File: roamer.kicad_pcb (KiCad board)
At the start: 4 copper layers, 39 x 99 mm, 103 parts, among them J1 Conn_Coaxial_Small, J2 JSTPH, J3 Conn_02x05_Odd_Even, J4 Conn_Coaxial_Small, J5 Conn_02x05_Odd_Even, J8 MEM2075-00-140-01-A, Q3 DMP2070UQ-7, SW1 KMR2, U1 2MB Flash, U2 AP2112K-3.3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

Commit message: Adding finishing touches
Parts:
- removed TP7, TP8, TP9: TestPoint, TestPoint:TestPoint_Loop_D2.50mm_Drill1.0mm
- added +BAT: TestPoint, TestPoint:TestPoint_Loop_D2.50mm_Drill1.0mm, F.Cu at (253.0, 174.8)
- added +VBUS: TestPoint, TestPoint:TestPoint_Loop_D2.50mm_Drill1.0mm, F.Cu at (253.0, 170.2)
- added 3V3: TestPoint, TestPoint:TestPoint_Loop_D2.50mm_Drill1.0mm, F.Cu at (240.0, 173.5)
- added G***: LOGO, LOGO, F.Cu at (236.2, 169.2)
- AREF <> 3V3: renamed from JP1
- IN <> +BATT: renamed from JP3
- LoRa 433: renamed from U9
- LoRa 900: renamed from U4
- moved R9 3.64 mm to (221.0, 164.2)
- renumbered U7 to BME, U8 to INA
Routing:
- net /Power - Management/IN-: track 27.2 -> 17.3 mm
- net VBUS: track 58.3 -> 65.8 mm
- net Net-(MCU1-PB01): track 20.2 -> 16.5 mm
- net +BATT: track 85.2 -> 82.6 mm, vias 2 -> 3
- net GND: track 147.2 -> 147.4 mm, vias 118 -> 115
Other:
- board text added: "433 Mhz"
- board text added: "900 Mhz"
- board text added: "BATT"
- board text added: "ROAMER"
- board text added: "SWD"
- board text added: "catbranchman"
- board text added: "rev 1"

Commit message: Creating fab package
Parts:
- added TP6: GND Testpoint, TestPoint:TestPoint_Loop_D2.50mm_Drill1.0mm, F.Cu at (221.8, 156.2)
- JP1: renamed from AREF <> 3V3
- JP3: renamed from IN <> +BATT
- TP1: renamed from +VBUS; value TestPoint -> VBUS Testpoint
- TP2: renamed from +BAT; value TestPoint -> Batt Testpoint
- TP3: value TestPoint -> D+ Testpoint
- TP4: value TestPoint -> D- TestPoint
- TP7: renamed from 3V3; value TestPoint -> 3V3 Testpoint
- U4: renamed from LoRa 900
- U9: renamed from LoRa 433
- moved G*** 0.25 mm to (236.0, 169.2)
- renumbered BME to U7, INA to U8
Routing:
- net GND: track 147.4 -> 151.1 mm, vias 115 -> 108
- net Net-(MCU1-PB01): track 16.5 -> 20.2 mm
- net /Bus - SPI/SPI.SCK: track 62.3 -> 63.9 mm
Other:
- board text added: "433M"
- board text added: "915M"
- board text removed: "433 Mhz"
- board text removed: "900 Mhz"

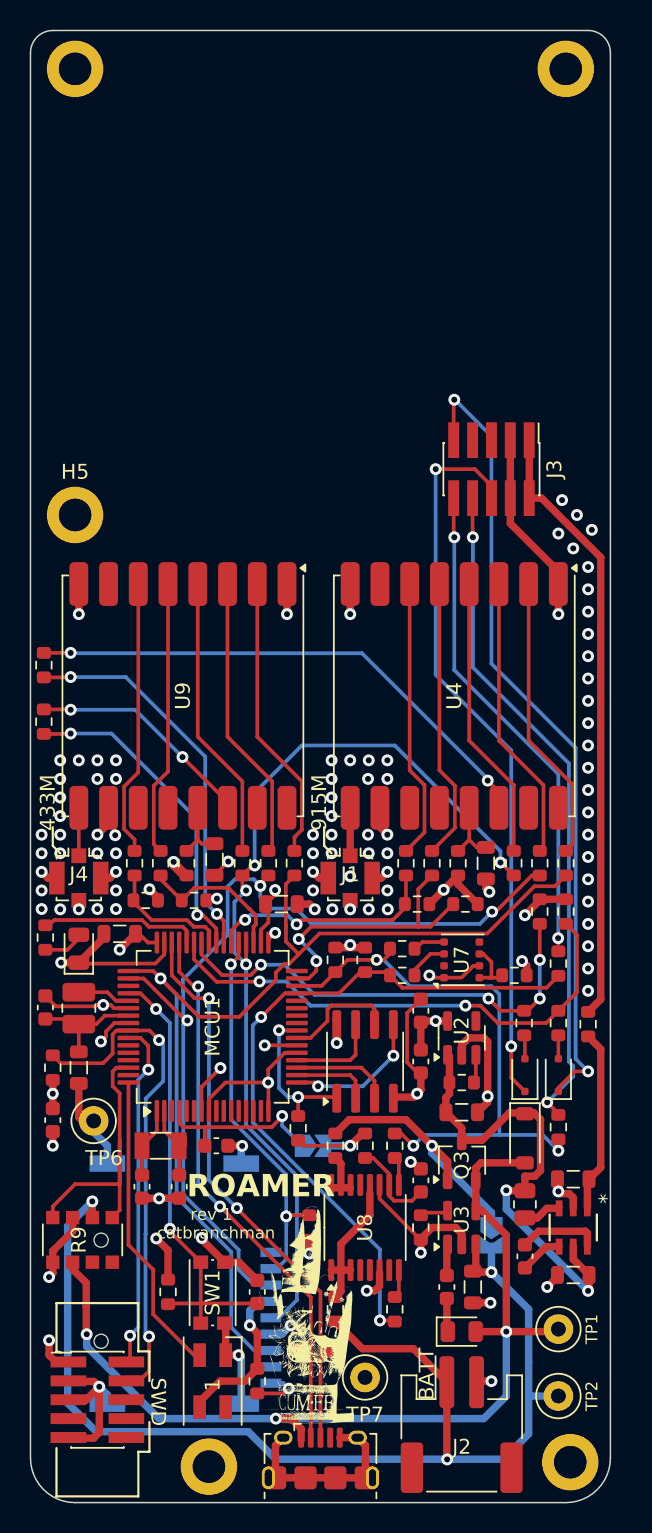
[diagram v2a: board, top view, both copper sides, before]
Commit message: Updating silkscreen comments
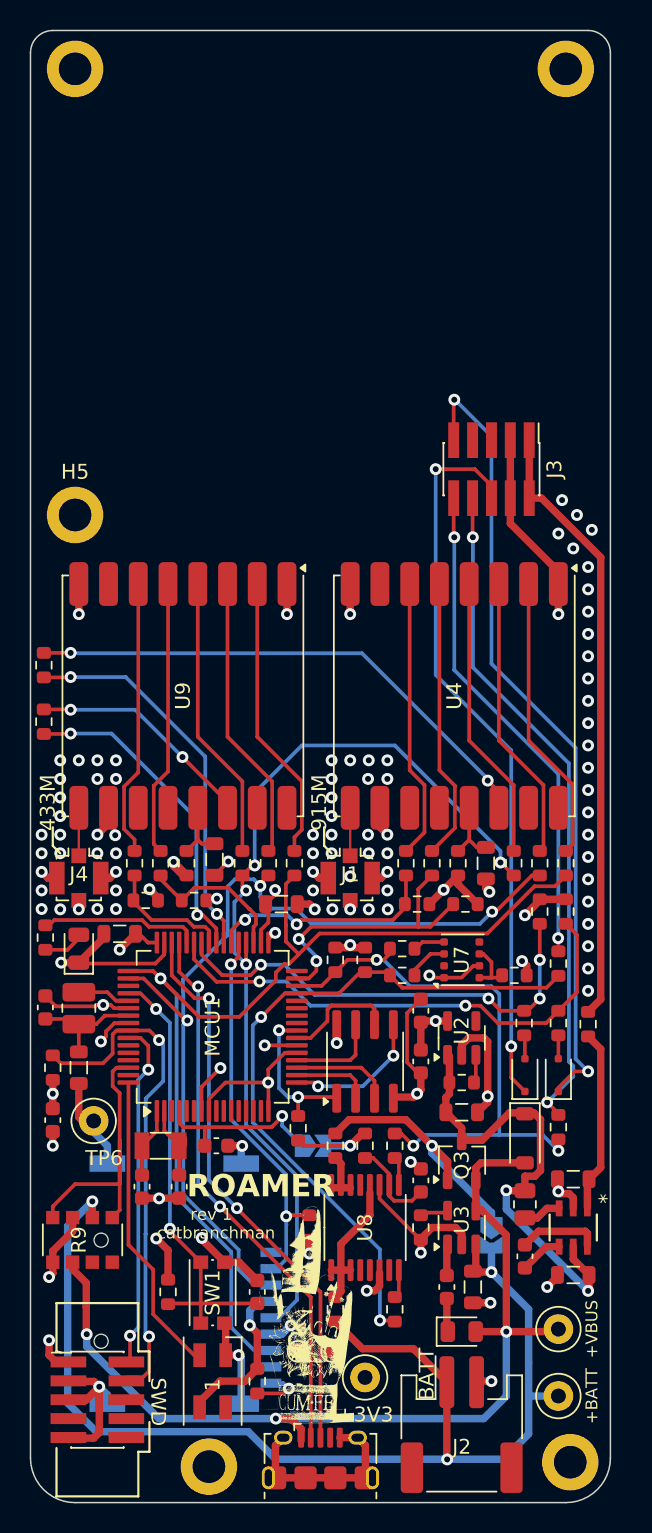
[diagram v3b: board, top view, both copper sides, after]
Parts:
- AREF <> 3V3: renamed from JP1
- IN- <> BATT+: renamed from JP3
- renumbered TP7 to +3V3, TP2 to +BATT, TP1 to +VBUS
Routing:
- net Net-(J4-In): track 2.65 -> 3.22 mm
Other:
- board text added: "2"
- board text added: "3"
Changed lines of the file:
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@@
 		(descr "wire loop as test point, loop diameter 2.5mm, hole diameter 1.0mm")
 		(tags "test point wire loop bead")
-		(property "Reference" "TP1"
+		(property "Reference" "+VBUS"
 			(at 2.25 0 90)
 			(layer "F.SilkS" knockout)
@@
 		(descr "wire loop as test point, loop diameter 2.5mm, hole diameter 1.0mm")
 		(tags "test point wire loop bead")
-		(property "Reference" "TP2"
+		(property "Reference" "+BATT"
 			(at 2.25 0 90)
 			(unlocked yes)
@@
 		(descr "wire loop as test point, loop diameter 2.5mm, hole diameter 1.0mm")
 		(tags "test point wire loop bead")
-		(property "Reference" "TP7"
+		(property "Reference" "+3V3"
 			(at 0 2.5 0)
 			(layer "F.SilkS" knockout)
@@
 		(descr "SMD Solder Jumper, 1x1.5mm Triangular Pads, 0.3mm gap, open")
 		(tags "solder jumper open")
-		(property "Reference" "JP1"
+		(property "Reference" "AREF <> 3V3"
 			(at 3.75 -1.91875 0)
 			(layer "B.SilkS" knockout)
@@
 		(descr "SMD Solder Jumper, 1x1.5mm Triangular Pads, 0.3mm gap, open")
 		(tags "solder jumper open")
-		(property "Reference" "JP3"
+		(property "Reference" "IN- <> BATT+"
 			(at -2.44375 4.25 180)
 			(layer "B.SilkS" knockout)
@@
 		(layer "Edge.Cuts")
 	)
+	(gr_text "2"
+		(at 239.5 86 90)
+		(layer "In1.Cu")
+		(effects
+			(font
+				(size 1 1)
+				(thickness 0.25)
+				(bold yes)
+			)
+			(justify left bottom)
+		)
+	)
+	(gr_text "3"
+		(at 237 84.75 90)
+		(layer "In2.Cu")
+		(effects
+			(font
+				(size 1 1)
+				(thickness 0.25)
+				(bold yes)
+			)
+			(justify left bottom mirror)
+		)
+	)
 	(gr_text "SWD"
 		(at 225.5 173.5 270)
@@
 		(start 239 138.41875)
 		(end 239 135.19375)
-		(width 0.5)
+		(width 0.156)
 		(layer "F.Cu")
 		(net 14)
@@
 	)
 	(segment
-		(start 220.75 135.76875)
-		(end 220.75 138.41875)
-		(width 0.25)
+		(start 220.75 138.41875)
+		(end 220.75 135.19375)
+		(width 0.156)
 		(layer "F.Cu")
 		(net 22)
@@
 	)
 	(zone
+		(net 0)
+		(net_name "")
+		(layer "In1.Cu")
+		(hatch edge 0.5)
+		(connect_pads
+			(clearance 0)
+		)
+		(min_thickness 0.25)
+		(filled_areas_thickness no)
+		(keepout
+			(tracks not_allowed)
+			(vias not_allowed)
+			(pads not_allowed)
+			(copperpour not_allowed)
+			(footprints allowed)
+		)
+		(fill
+			(thermal_gap 0.5)
+			(thermal_bridge_width 0.5)
+		)
+		(polygon
+			(pts
+				(xy 240.25 83.25) (xy 240.25 87.25) (xy 237.75 87.25) (xy 237.75 83.25)
+			)
+		)
+	)
+	(zone
 		(net 2)
 		(net_name "GND")
@@
 			)
 		)
+	)
+	(zone
+		(net 0)
+		(net_name "")
+		(layer "In2.Cu")
+		(hatch edge 0.5)
+		(connect_pads
+			(clearance 0)
+		)
+		(min_thickness 0.25)
+		(filled_areas_thickness no)
+		(keepout
+			(tracks not_allowed)
+			(vias not_allowed)
+			(pads not_allowed)
+			(copperpour not_allowed)
+			(footprints allowed)
+		)
+		(fill
+			(thermal_gap 0.5)
+			(thermal_bridge_width 0.5)
+		)
+		(polygon
+			(pts
+				(xy 240.25 83.25) (xy 240.25 87.25) (xy 235 87.25) (xy 235 83.25)
+			)
+		)

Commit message: Updating tags
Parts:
- renumbered TP6 to GND
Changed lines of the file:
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@@
 		(descr "wire loop as test point, loop diameter 2.5mm, hole diameter 1.0mm")
 		(tags "test point wire loop bead")
-		(property "Reference" "TP6"
-			(at 0.7 2.5 0)
-			(layer "F.SilkS")
+		(property "Reference" "GND"
+			(at 0 2.5 0)
+			(layer "F.SilkS" knockout)
 			(effects
 				(font
